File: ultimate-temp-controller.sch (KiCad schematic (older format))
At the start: 0 parts

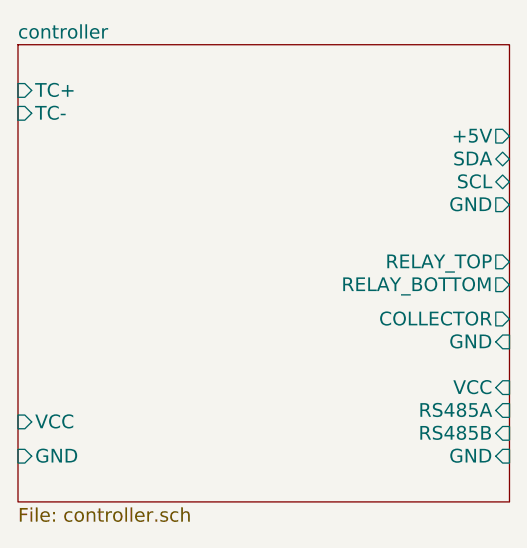
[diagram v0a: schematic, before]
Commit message: Add open drain output, shuffle other connectors around
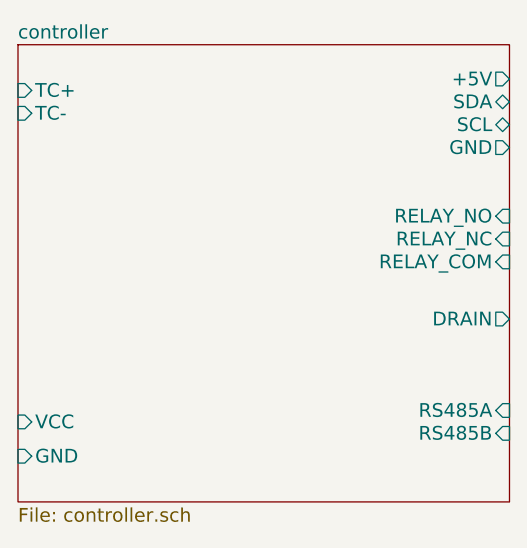
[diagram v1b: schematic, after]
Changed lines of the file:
@@
 F4 "VCC" I L 1400 3750 60
 F5 "GND" I L 1400 3900 60
-F6 "VCC" I R 3550 3600 60
-F7 "RS485A" I R 3550 3700 60
-F8 "RS485B" I R 3550 3800 60
-F9 "GND" I R 3550 3900 60
-F10 "GND" I R 3550 3400 60
-F11 "COLLECTOR" O R 3550 3300 60
-F12 "RELAY_TOP" O R 3550 3050 60
-F13 "RELAY_BOTTOM" O R 3550 3150 60
-F14 "+5V" O R 3550 2500 60
-F15 "SDA" B R 3550 2600 60
-F16 "SCL" B R 3550 2700 60
-F17 "GND" O R 3550 2800 60
+F6 "RS485A" I R 3550 3700 60
+F7 "RS485B" I R 3550 3800 60
+F8 "DRAIN" O R 3550 3300 60
+F9 "+5V" O R 3550 2250 60
+F10 "SDA" B R 3550 2350 60
+F11 "SCL" B R 3550 2450 60
+F12 "GND" O R 3550 2550 60
+F13 "RELAY_NO" I R 3550 2850 60
+F14 "RELAY_COM" I R 3550 3050 60
+F15 "RELAY_NC" I R 3550 2950 60
 $EndSheet
 $EndSCHEMATC
